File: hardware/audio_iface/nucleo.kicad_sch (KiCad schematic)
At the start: 1 part, among them U101 NUCLEO_L476RG

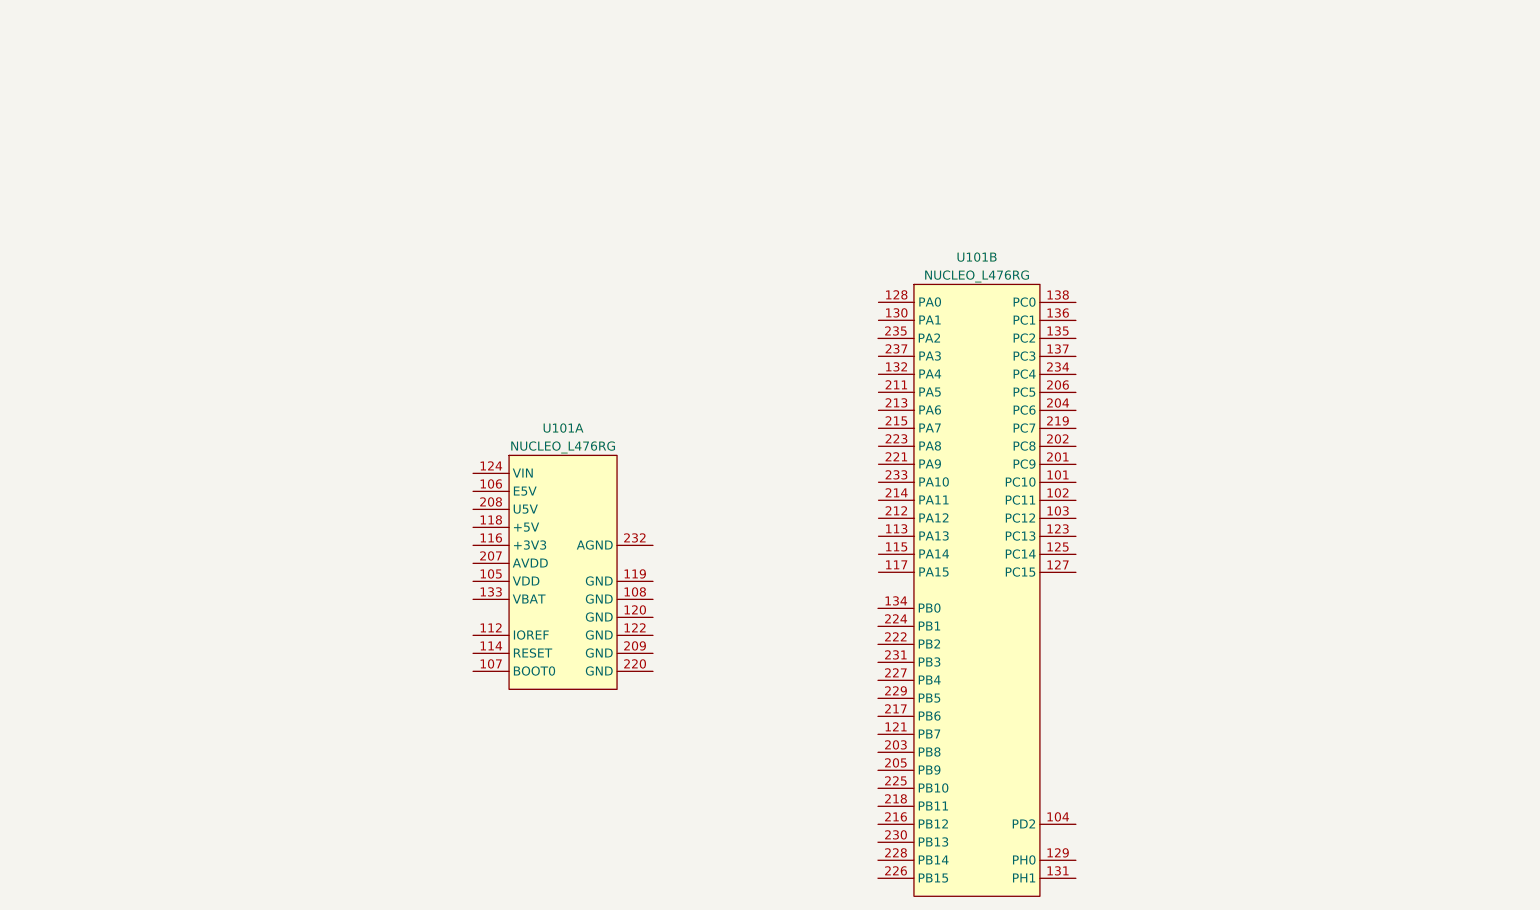
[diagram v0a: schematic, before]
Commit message: added some connections
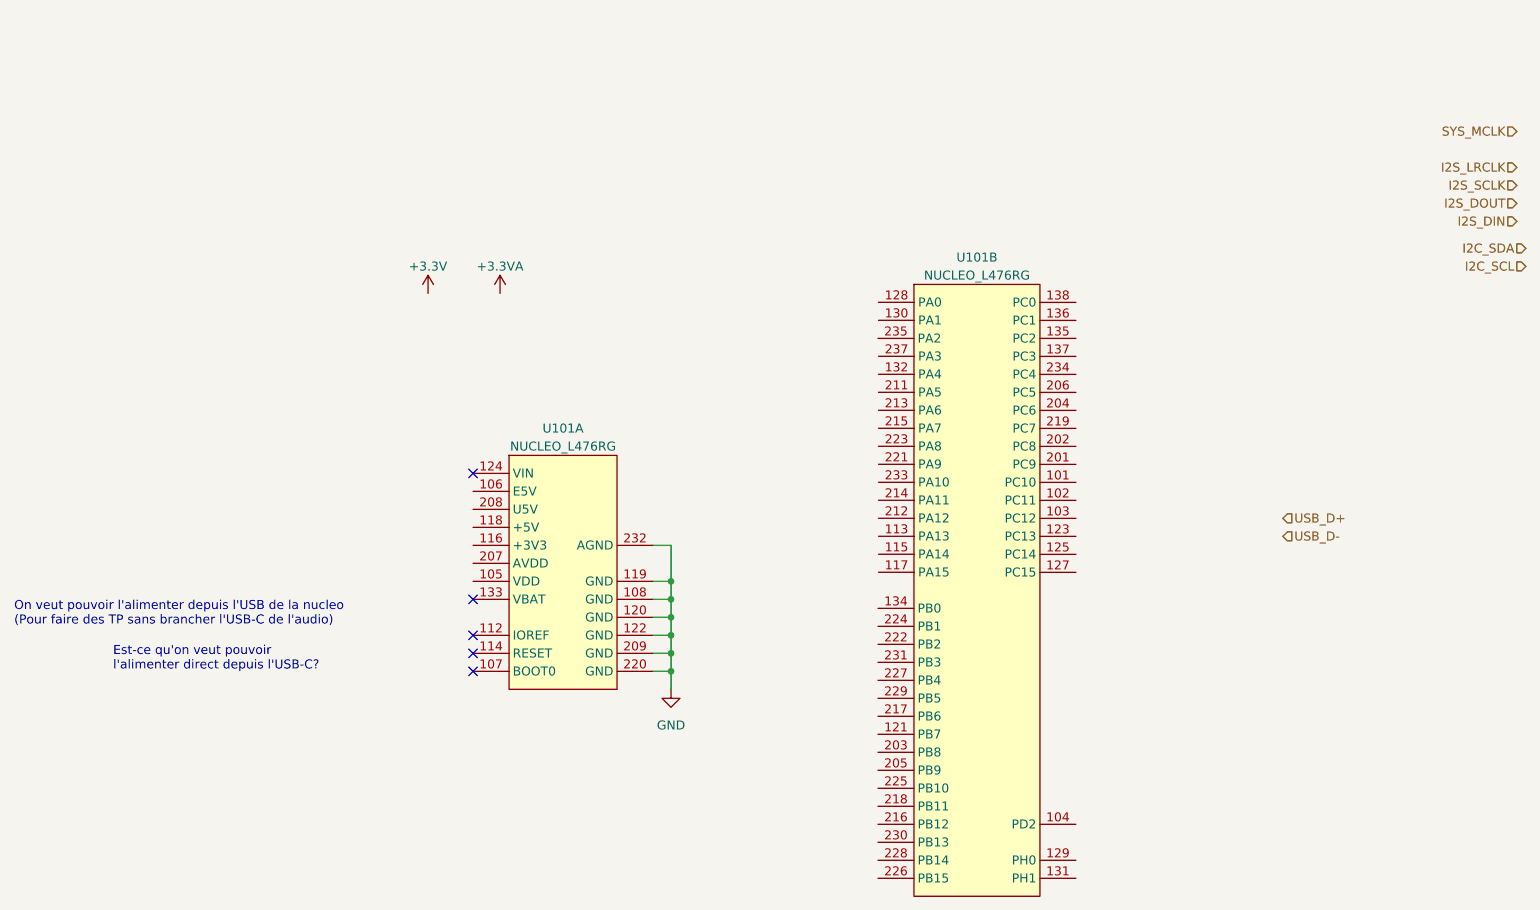
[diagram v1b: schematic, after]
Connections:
- net GND: now reaches U101.108 (GND)
- net GND: now also U101.119 (GND), U101.120 (GND), U101.122 (GND), U101.209 (GND), U101.220 (GND), U101.232 (AGND)
- no-connect marks 0 -> 5
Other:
- note added: "Est-ce qu'on veut pouvoir l'alimenter direct depuis l'USB-C?"
- note added: "On veut pouvoir l'alimenter depuis l'USB de la nucleo (Pour faire des TP sans brancher l'USB-C de l'audio)"
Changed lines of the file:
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@@
 (kicad_sch (version 20230121) (generator eeschema)
   (paper "A4")
+  (junction (at 120.65 111.76) (diameter 0) (color 0 0 0 0)
+  )
+  (junction (at 120.65 106.68) (diameter 0) (color 0 0 0 0)
+  )
+  (junction (at 120.65 116.84) (diameter 0) (color 0 0 0 0)
+  )
+  (junction (at 120.65 119.38) (diameter 0) (color 0 0 0 0)
+  )
+  (junction (at 120.65 109.22) (diameter 0) (color 0 0 0 0)
+  )
+  (junction (at 120.65 114.3) (diameter 0) (color 0 0 0 0)
+  )
+  (no_connect (at 92.71 114.3))
+  (no_connect (at 92.71 119.38))
+  (no_connect (at 92.71 91.44))
+  (no_connect (at 92.71 109.22))
+  (no_connect (at 92.71 116.84))
+  (wire (pts (xy 118.11 106.68) (xy 120.65 106.68))
+    (stroke (width 0) (type default))
+  )
+  (wire (pts (xy 120.65 111.76) (xy 120.65 109.22))
+    (stroke (width 0) (type default))
+  )
+  (wire (pts (xy 118.11 109.22) (xy 120.65 109.22))
+    (stroke (width 0) (type default))
+  )
+  (wire (pts (xy 118.11 114.3) (xy 120.65 114.3))
+    (stroke (width 0) (type default))
+  )
+  (wire (pts (xy 118.11 111.76) (xy 120.65 111.76))
+    (stroke (width 0) (type default))
+  )
+  (wire (pts (xy 120.65 114.3) (xy 120.65 111.76))
+    (stroke (width 0) (type default))
+  )
+  (wire (pts (xy 120.65 116.84) (xy 120.65 114.3))
+    (stroke (width 0) (type default))
+  )
+  (wire (pts (xy 120.65 101.6) (xy 118.11 101.6))
+    (stroke (width 0) (type default))
+  )
+  (wire (pts (xy 120.65 109.22) (xy 120.65 106.68))
+    (stroke (width 0) (type default))
+  )
+  (wire (pts (xy 118.11 119.38) (xy 120.65 119.38))
+    (stroke (width 0) (type default))
+  )
+  (wire (pts (xy 120.65 119.38) (xy 120.65 116.84))
+    (stroke (width 0) (type default))
+  )
+  (wire (pts (xy 120.65 121.92) (xy 120.65 119.38))
+    (stroke (width 0) (type default))
+  )
+  (wire (pts (xy 120.65 106.68) (xy 120.65 101.6))
+    (stroke (width 0) (type default))
+  )
+  (wire (pts (xy 118.11 116.84) (xy 120.65 116.84))
+    (stroke (width 0) (type default))
+  )
+  (text "On veut pouvoir l'alimenter depuis l'USB de la nucleo\n(Pour faire des TP sans brancher l'USB-C de l'audio)"
+    (at 27.94 113.03 0)
+    (effects (font (size 1.27 1.27)) (justify left bottom))
+  )
+  (text "Est-ce qu'on veut pouvoir \nl'alimenter direct depuis l'USB-C?"
+    (at 41.91 119.38 0)
+    (effects (font (size 1.27 1.27)) (justify left bottom))
+  )
+  (hierarchical_label "I2S_SCLK" (shape input) (at 240.03 50.8 180) (fields_autoplaced)
+    (effects (font (size 1.27 1.27)) (justify right))
+  )
+  (hierarchical_label "I2S_DIN" (shape input) (at 240.03 55.88 180) (fields_autoplaced)
+    (effects (font (size 1.27 1.27)) (justify right))
+  )
+  (hierarchical_label "I2S_DOUT" (shape input) (at 240.03 53.34 180) (fields_autoplaced)
+    (effects (font (size 1.27 1.27)) (justify right))
+  )
+  (hierarchical_label "I2C_SCL" (shape input) (at 241.3 62.23 180) (fields_autoplaced)
+    (effects (font (size 1.27 1.27)) (justify right))
+  )
+  (hierarchical_label "I2C_SDA" (shape input) (at 241.3 59.69 180) (fields_autoplaced)
+    (effects (font (size 1.27 1.27)) (justify right))
+  )
+  (hierarchical_label "USB_D-" (shape input) (at 207.01 100.33 0) (fields_autoplaced)
+    (effects (font (size 1.27 1.27)) (justify left))
+  )
+  (hierarchical_label "SYS_MCLK" (shape input) (at 240.03 43.18 180) (fields_autoplaced)
+    (effects (font (size 1.27 1.27)) (justify right))
+  )
+  (hierarchical_label "USB_D+" (shape input) (at 207.01 97.79 0) (fields_autoplaced)
+    (effects (font (size 1.27 1.27)) (justify left))
+  )
+  (hierarchical_label "I2S_LRCLK" (shape input) (at 240.03 48.26 180) (fields_autoplaced)
+    (effects (font (size 1.27 1.27)) (justify right))
+  )
+  (symbol (lib_id "power:+3.3VA") (at 96.52 66.04 0) (unit 1)
+    (in_bom yes) (on_board yes) (dnp no) (fields_autoplaced)
+    (property "Reference" "#PWR0203" (at 96.52 69.85 0)
+      (effects (font (size 1.27 1.27)) hide)
+    )
+    (property "Value" "+3.3VA" (at 96.52 62.23 0)
+      (effects (font (size 1.27 1.27)))
+    )
+    (property "Footprint" "" (at 96.52 66.04 0)
+      (effects (font (size 1.27 1.27)) hide)
+    )
+    (property "Datasheet" "" (at 96.52 66.04 0)
+      (effects (font (size 1.27 1.27)) hide)
+    )
+    (pin "1")
+    (instances
+      (project "audio_iface"
+        (path "/84adbf2e-65c7-4710-86f9-725cae0256c9/cdd727d1-dc6e-479c-822a-c88c05fafe87"
+          (reference "#PWR0203") (unit 1)
+        )
+      )
+    )
+  )
   (symbol (lib_id "WITNS_ST:NUCLEO_L476RG") (at 163.83 107.95 0) (unit 2)
     (in_bom yes) (on_board yes) (dnp no) (fields_autoplaced)
@@
     )
   )
+  (symbol (lib_id "power:GND") (at 120.65 121.92 0) (unit 1)
+    (in_bom yes) (on_board yes) (dnp no) (fields_autoplaced)
+    (property "Reference" "#PWR0201" (at 120.65 128.27 0)
+      (effects (font (size 1.27 1.27)) hide)
+    )
+    (property "Value" "GND" (at 120.65 127 0)
+      (effects (font (size 1.27 1.27)))
+    )
+    (property "Footprint" "" (at 120.65 121.92 0)
+      (effects (font (size 1.27 1.27)) hide)
+    )
+    (property "Datasheet" "" (at 120.65 121.92 0)
+      (effects (font (size 1.27 1.27)) hide)
+    )
+    (pin "1")
+    (instances
+      (project "audio_iface"
+        (path "/84adbf2e-65c7-4710-86f9-725cae0256c9/cdd727d1-dc6e-479c-822a-c88c05fafe87"
+          (reference "#PWR0201") (unit 1)
+        )
+      )
+    )
+  )
   (symbol (lib_id "WITNS_ST:NUCLEO_L476RG") (at 105.41 105.41 0) (unit 1)
     (in_bom yes) (on_board yes) (dnp no) (fields_autoplaced)
@@
         )
       )
+    )
+  )
+  (symbol (lib_id "power:+3.3V") (at 86.36 66.04 0) (unit 1)
+    (in_bom yes) (on_board yes) (dnp no) (fields_autoplaced)
+    (property "Reference" "#PWR0202" (at 86.36 69.85 0)
+      (effects (font (size 1.27 1.27)) hide)
+    )
+    (property "Value" "+3.3V" (at 86.36 62.23 0)
+      (effects (font (size 1.27 1.27)))
+    )
+    (property "Footprint" "" (at 86.36 66.04 0)
+      (effects (font (size 1.27 1.27)) hide)
+    )
+    (property "Datasheet" "" (at 86.36 66.04 0)
+      (effects (font (size 1.27 1.27)) hide)
+    )
+    (pin "1")
+    (instances
+      (project "audio_iface"
+        (path "/84adbf2e-65c7-4710-86f9-725cae0256c9/cdd727d1-dc6e-479c-822a-c88c05fafe87"
+          (reference "#PWR0202") (unit 1)
+        )
+      )

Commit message: Added LEDs
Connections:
- net +3.3V: now also U101.105 (VDD)
- net +3.3VA: now also U101.207 (AVDD)
- net USB_D+: now also U101.212 (PA12)
- net USB_D-: now also U101.214 (PA11)
- no-connect marks 5 -> 9
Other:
- note added: "VDD is after the IDD jumper; +3V3 is just before"
- moved on the sheet: U101B
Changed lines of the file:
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@@
   (junction (at 120.65 114.3) (diameter 0) (color 0 0 0 0)
   )
+  (no_connect (at 92.71 93.98))
+  (no_connect (at 92.71 101.6))
   (no_connect (at 92.71 114.3))
   (no_connect (at 92.71 119.38))
+  (no_connect (at 92.71 99.06))
   (no_connect (at 92.71 91.44))
   (no_connect (at 92.71 109.22))
+  (no_connect (at 92.71 96.52))
   (no_connect (at 92.71 116.84))
+  (wire (pts (xy 92.71 106.68) (xy 77.47 106.68))
+    (stroke (width 0) (type default))
+  )
   (wire (pts (xy 118.11 106.68) (xy 120.65 106.68))
     (stroke (width 0) (type default))
@@
     (stroke (width 0) (type default))
   )
+  (wire (pts (xy 85.09 104.14) (xy 85.09 102.87))
+    (stroke (width 0) (type default))
+  )
   (wire (pts (xy 118.11 114.3) (xy 120.65 114.3))
     (stroke (width 0) (type default))
@@
     (stroke (width 0) (type default))
   )
+  (wire (pts (xy 85.09 104.14) (xy 92.71 104.14))
+    (stroke (width 0) (type default))
+  )
   (wire (pts (xy 120.65 109.22) (xy 120.65 106.68))
     (stroke (width 0) (type default))
   )
   (wire (pts (xy 118.11 119.38) (xy 120.65 119.38))
+    (stroke (width 0) (type default))
+  )
+  (wire (pts (xy 77.47 106.68) (xy 77.47 102.87))
     (stroke (width 0) (type default))
   )
@@
     (effects (font (size 1.27 1.27)) (justify left bottom))
   )
+  (text "VDD is after the IDD jumper;\n+3V3 is just before" (at 50.8 93.98 0)
+    (effects (font (size 1.27 1.27)) (justify left bottom))
+  )
   (text "Est-ce qu'on veut pouvoir \nl'alimenter direct depuis l'USB-C?"
     (at 41.91 119.38 0)
@@
     (effects (font (size 1.27 1.27)) (justify right))
   )
+  (hierarchical_label "VU_MOSI" (shape input) (at 232.41 121.92 180) (fields_autoplaced)
+    (effects (font (size 1.27 1.27)) (justify right))
+  )
   (hierarchical_label "I2S_DIN" (shape input) (at 240.03 55.88 180) (fields_autoplaced)
     (effects (font (size 1.27 1.27)) (justify right))
@@
     (effects (font (size 1.27 1.27)) (justify right))
   )
+  (hierarchical_label "VU_nCS" (shape input) (at 232.41 116.84 180) (fields_autoplaced)
+    (effects (font (size 1.27 1.27)) (justify right))
+  )
   (hierarchical_label "I2C_SCL" (shape input) (at 241.3 62.23 180) (fields_autoplaced)
     (effects (font (size 1.27 1.27)) (justify right))
@@
     (effects (font (size 1.27 1.27)) (justify right))
   )
-  (hierarchical_label "USB_D-" (shape input) (at 207.01 100.33 0) (fields_autoplaced)
-    (effects (font (size 1.27 1.27)) (justify left))
+  (hierarchical_label "VU_MISO" (shape input) (at 232.41 124.46 180) (fields_autoplaced)
+    (effects (font (size 1.27 1.27)) (justify right))
+  )
+  (hierarchical_label "VU_nRESET" (shape input) (at 232.41 139.7 180) (fields_autoplaced)
+    (effects (font (size 1.27 1.27)) (justify right))
+  )
+  (hierarchical_label "USB_D-" (shape input) (at 152.4 95.25 180) (fields_autoplaced)
+    (effects (font (size 1.27 1.27)) (justify right))
   )
   (hierarchical_label "SYS_MCLK" (shape input) (at 240.03 43.18 180) (fields_autoplaced)
     (effects (font (size 1.27 1.27)) (justify right))
   )
-  (hierarchical_label "USB_D+" (shape input) (at 207.01 97.79 0) (fields_autoplaced)
-    (effects (font (size 1.27 1.27)) (justify left))
+  (hierarchical_label "USB_D+" (shape input) (at 152.4 97.79 180) (fields_autoplaced)
+    (effects (font (size 1.27 1.27)) (justify right))
+  )
+  (hierarchical_label "VU_SCK" (shape input) (at 232.41 119.38 180) (fields_autoplaced)
+    (effects (font (size 1.27 1.27)) (justify right))
   )
   (hierarchical_label "I2S_LRCLK" (shape input) (at 240.03 48.26 180) (fields_autoplaced)
     (effects (font (size 1.27 1.27)) (justify right))
   )
-  (symbol (lib_id "power:+3.3VA") (at 96.52 66.04 0) (unit 1)
-    (in_bom yes) (on_board yes) (dnp no) (fields_autoplaced)
-    (property "Reference" "#PWR0203" (at 96.52 69.85 0)
-      (effects (font (size 1.27 1.27)) hide)
-    )
-    (property "Value" "+3.3VA" (at 96.52 62.23 0)
-      (effects (font (size 1.27 1.27)))
-    )
-    (property "Footprint" "" (at 96.52 66.04 0)
-      (effects (font (size 1.27 1.27)) hide)
-    )
-    (property "Datasheet" "" (at 96.52 66.04 0)
+  (symbol (lib_id "power:+3.3VA") (at 85.09 102.87 0) (unit 1)
+    (in_bom yes) (on_board yes) (dnp no) (fields_autoplaced)
+    (property "Reference" "#PWR0202" (at 85.09 106.68 0)
+      (effects (font (size 1.27 1.27)) hide)
+    )
+    (property "Value" "+3.3VA" (at 85.09 99.06 0)
+      (effects (font (size 1.27 1.27)))
+    )
+    (property "Footprint" "" (at 85.09 102.87 0)
+      (effects (font (size 1.27 1.27)) hide)
+    )
+    (property "Datasheet" "" (at 85.09 102.87 0)
       (effects (font (size 1.27 1.27)) hide)
     )
@@
       (project "audio_iface"
         (path "/84adbf2e-65c7-4710-86f9-725cae0256c9/cdd727d1-dc6e-479c-822a-c88c05fafe87"
-          (reference "#PWR0203") (unit 1)
-        )
-      )
-    )
-  )
-  (symbol (lib_id "WITNS_ST:NUCLEO_L476RG") (at 163.83 107.95 0) (unit 2)
-    (in_bom yes) (on_board yes) (dnp no) (fields_autoplaced)
-    (property "Reference" "U101" (at 163.83 60.96 0)
-      (effects (font (size 1.27 1.27)))
-    )
-    (property "Value" "NUCLEO_L476RG" (at 163.83 63.5 0)
-      (effects (font (size 1.27 1.27)))
-    )
-    (property "Footprint" "WITNS:ST_NUCLEO_64" (at 163.83 85.09 0)
-      (effects (font (size 1.27 1.27)) hide)
-    )
-    (property "Datasheet" "" (at 163.83 85.09 0)
+          (reference "#PWR0202") (unit 1)
+        )
+      )
+    )
+  )
+  (symbol (lib_name "NUCLEO_L476RG_1") (lib_id "WITNS_ST:NUCLEO_L476RG") (at 166.37 107.95 0) (unit 2)
+    (in_bom yes) (on_board yes) (dnp no) (fields_autoplaced)
+    (property "Reference" "U101" (at 166.37 60.96 0)
+      (effects (font (size 1.27 1.27)))
+    )
+    (property "Value" "NUCLEO_L476RG" (at 166.37 63.5 0)
+      (effects (font (size 1.27 1.27)))
+    )
+    (property "Footprint" "WITNS:ST_NUCLEO_64" (at 166.37 85.09 0)
+      (effects (font (size 1.27 1.27)) hide)
+    )
+    (property "Datasheet" "" (at 166.37 85.09 0)
       (effects (font (size 1.27 1.27)) hide)
     )
@@
   (symbol (lib_id "power:GND") (at 120.65 121.92 0) (unit 1)
     (in_bom yes) (on_board yes) (dnp no) (fields_autoplaced)
-    (property "Reference" "#PWR0201" (at 120.65 128.27 0)
+    (property "Reference" "#PWR0203" (at 120.65 128.27 0)
       (effects (font (size 1.27 1.27)) hide)
     )
@@
       (project "audio_iface"
         (path "/84adbf2e-65c7-4710-86f9-725cae0256c9/cdd727d1-dc6e-479c-822a-c88c05fafe87"
-          (reference "#PWR0201") (unit 1)
+          (reference "#PWR0203") (unit 1)
         )
       )
@@
     )
   )
-  (symbol (lib_id "power:+3.3V") (at 86.36 66.04 0) (unit 1)
-    (in_bom yes) (on_board yes) (dnp no) (fields_autoplaced)
-    (property "Reference" "#PWR0202" (at 86.36 69.85 0)
-      (effects (font (size 1.27 1.27)) hide)
-    )
-    (property "Value" "+3.3V" (at 86.36 62.23 0)
-      (effects (font (size 1.27 1.27)))
-    )
-    (property "Footprint" "" (at 86.36 66.04 0)
-      (effects (font (size 1.27 1.27)) hide)
-    )
-    (property "Datasheet" "" (at 86.36 66.04 0)
+  (symbol (lib_id "power:+3.3V") (at 77.47 102.87 0) (unit 1)
+    (in_bom yes) (on_board yes) (dnp no) (fields_autoplaced)
+    (property "Reference" "#PWR0201" (at 77.47 106.68 0)
+      (effects (font (size 1.27 1.27)) hide)
+    )
+    (property "Value" "+3.3V" (at 77.47 99.06 0)
+      (effects (font (size 1.27 1.27)))
+    )
+    (property "Footprint" "" (at 77.47 102.87 0)
+      (effects (font (size 1.27 1.27)) hide)
+    )
+    (property "Datasheet" "" (at 77.47 102.87 0)
       (effects (font (size 1.27 1.27)) hide)
     )
@@
       (project "audio_iface"
         (path "/84adbf2e-65c7-4710-86f9-725cae0256c9/cdd727d1-dc6e-479c-822a-c88c05fafe87"
-          (reference "#PWR0202") (unit 1)
-        )
-      )
+          (reference "#PWR0201") (unit 1)
+        )
+      )
